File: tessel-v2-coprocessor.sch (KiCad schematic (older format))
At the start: 46 parts, among them J401 CONN_02X05, J402 USB-micro-TH, J403 MODULE_HEADER, J404 MODULE_HEADER, J405 CONN_01X01, SW401 SW_PUSH, U401 SAMD21G14A-MU, X401 FC-135

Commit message: annotated
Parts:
- gave numbers to parts that had none: 4
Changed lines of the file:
@@
 $EndComp
 $Comp
-L GND #PWR0110
+L GND #PWR408
 U 1 1 548F9730
 P 4800 8050
-F 0 "#PWR0110" H 4800 8050 30  0001 C CNN
+F 0 "#PWR408" H 4800 8050 30  0001 C CNN
 F 1 "GND" H 4800 7980 30  0001 C CNN
 F 2 "" H 4800 8050 60  0000 C CNN
@@
 $EndComp
 $Comp
-L GND #PWR0111
+L GND #PWR410
 U 1 1 548F973F
 P 6000 8100
-F 0 "#PWR0111" H 6000 8100 30  0001 C CNN
+F 0 "#PWR410" H 6000 8100 30  0001 C CNN
 F 1 "GND" H 6000 8030 30  0001 C CNN
 F 2 "" H 6000 8100 60  0000 C CNN
@@
 VDDCORE
 $Comp
-L GND #PWR0112
+L GND #PWR417
 U 1 1 548FA205
 P 9400 3700
-F 0 "#PWR0112" H 9400 3700 30  0001 C CNN
+F 0 "#PWR417" H 9400 3700 30  0001 C CNN
 F 1 "GND" H 9400 3630 30  0001 C CNN
 F 2 "" H 9400 3700 60  0000 C CNN
@@
 $EndComp
 $Comp
-L GND #PWR0113
+L GND #PWR416
 U 1 1 548FBD70
 P 9000 3700
-F 0 "#PWR0113" H 9000 3700 30  0001 C CNN
+F 0 "#PWR416" H 9000 3700 30  0001 C CNN
 F 1 "GND" H 9000 3630 30  0001 C CNN
 F 2 "" H 9000 3700 60  0000 C CNN
@@
 $EndComp
 $Comp
-L GND #PWR0114
+L GND #PWR414
 U 1 1 548FBD83
 P 7500 3700
-F 0 "#PWR0114" H 7500 3700 30  0001 C CNN
+F 0 "#PWR414" H 7500 3700 30  0001 C CNN
 F 1 "GND" H 7500 3630 30  0001 C CNN
 F 2 "" H 7500 3700 60  0000 C CNN
@@
 $EndComp
 $Comp
-L GND #PWR0115
+L GND #PWR413
 U 1 1 548FBD8A
 P 7100 3700
-F 0 "#PWR0115" H 7100 3700 30  0001 C CNN
+F 0 "#PWR413" H 7100 3700 30  0001 C CNN
 F 1 "GND" H 7100 3630 30  0001 C CNN
 F 2 "" H 7100 3700 60  0000 C CNN
@@
 $EndComp
 $Comp
-L GND #PWR0116
+L GND #PWR412
 U 1 1 548FBD9D
 P 6700 3700
-F 0 "#PWR0116" H 6700 3700 30  0001 C CNN
+F 0 "#PWR412" H 6700 3700 30  0001 C CNN
 F 1 "GND" H 6700 3630 30  0001 C CNN
 F 2 "" H 6700 3700 60  0000 C CNN
@@
 $EndComp
 $Comp
-L GND #PWR0117
+L GND #PWR411
 U 1 1 548FBDA4
 P 6300 3700
-F 0 "#PWR0117" H 6300 3700 30  0001 C CNN
+F 0 "#PWR411" H 6300 3700 30  0001 C CNN
 F 1 "GND" H 6300 3630 30  0001 C CNN
 F 2 "" H 6300 3700 60  0000 C CNN
@@
 $EndComp
 $Comp
-L GND #PWR0118
+L GND #PWR409
 U 1 1 548FBDB7
 P 5900 3700
-F 0 "#PWR0118" H 5900 3700 30  0001 C CNN
+F 0 "#PWR409" H 5900 3700 30  0001 C CNN
 F 1 "GND" H 5900 3630 30  0001 C CNN
 F 2 "" H 5900 3700 60  0000 C CNN
@@
 $EndComp
 $Comp
-L GND #PWR0119
+L GND #PWR415
 U 1 1 548FD791
 P 8000 8100
-F 0 "#PWR0119" H 8000 8100 30  0001 C CNN
+F 0 "#PWR415" H 8000 8100 30  0001 C CNN
 F 1 "GND" H 8000 8030 30  0001 C CNN
 F 2 "" H 8000 8100 60  0000 C CNN
@@
 $EndComp
 $Comp
-L GND #PWR0120
+L GND #PWR422
 U 1 1 54E6B173
 P 14600 7700
-F 0 "#PWR0120" H 14600 7700 30  0001 C CNN
+F 0 "#PWR422" H 14600 7700 30  0001 C CNN
 F 1 "GND" H 14600 7630 30  0001 C CNN
 F 2 "" H 14600 7700 60  0000 C CNN
@@
 3.3V_CP
 $Comp
-L GND #PWR0121
+L GND #PWR419
 U 1 1 54E6B4A0
 P 13600 7700
-F 0 "#PWR0121" H 13600 7700 30  0001 C CNN
+F 0 "#PWR419" H 13600 7700 30  0001 C CNN
 F 1 "GND" H 13600 7630 30  0001 C CNN
 F 2 "" H 13600 7700 60  0000 C CNN
@@
 NoConn ~ 1400 6400
 $Comp
-L GND #PWR0122
+L GND #PWR403
 U 1 1 54E6D866
 P 1300 6600
-F 0 "#PWR0122" H 1300 6350 60  0001 C CNN
+F 0 "#PWR403" H 1300 6350 60  0001 C CNN
 F 1 "GND" H 1300 6450 60  0000 C CNN
 F 2 "" H 1300 6600 60  0000 C CNN
@@
 3.3V_PORTA
 $Comp
-L GND #PWR0123
+L GND #PWR420
 U 1 1 54E753B7
 P 14200 2400
-F 0 "#PWR0123" H 14200 2150 60  0001 C CNN
+F 0 "#PWR420" H 14200 2150 60  0001 C CNN
 F 1 "GND" H 14200 2250 60  0000 C CNN
 F 2 "" H 14200 2400 60  0000 C CNN
@@
 $EndComp
 $Comp
-L GND #PWR0124
+L GND #PWR421
 U 1 1 54E753CD
 P 14300 4200
-F 0 "#PWR0124" H 14300 3950 60  0001 C CNN
+F 0 "#PWR421" H 14300 3950 60  0001 C CNN
 F 1 "GND" H 14300 4050 60  0000 C CNN
 F 2 "" H 14300 4200 60  0000 C CNN
@@
 PORT_A_G3
 $Comp
-L +5V #PWR0125
+L +5V #PWR404
 U 1 1 54E79A0D
 P 2600 1400
-F 0 "#PWR0125" H 2600 1490 20  0001 C CNN
+F 0 "#PWR404" H 2600 1490 20  0001 C CNN
 F 1 "+5V" H 2600 1550 30  0000 C CNN
 F 2 "" H 2600 1400 60  0000 C CNN
@@
 $EndComp
 $Comp
-L GND #PWR0126
+L GND #PWR405
 U 1 1 54E79A13
 P 2600 2100
-F 0 "#PWR0126" H 2600 1850 60  0001 C CNN
+F 0 "#PWR405" H 2600 1850 60  0001 C CNN
 F 1 "GND" H 2600 1950 60  0000 C CNN
 F 2 "" H 2600 2100 60  0000 C CNN
@@
 $EndComp
 $Comp
-L GND #PWR0127
+L GND #PWR406
 U 1 1 54E79A19
 P 2900 2500
-F 0 "#PWR0127" H 2900 2250 60  0001 C CNN
+F 0 "#PWR406" H 2900 2250 60  0001 C CNN
 F 1 "GND" H 2900 2350 60  0000 C CNN
 F 2 "" H 2900 2500 60  0000 C CNN
@@
 $EndComp
 $Comp
-L GND #PWR0128
+L GND #PWR401
 U 1 1 54E79A1F
 P 1300 3100
-F 0 "#PWR0128" H 1300 2850 60  0001 C CNN
+F 0 "#PWR401" H 1300 2850 60  0001 C CNN
 F 1 "GND" H 1300 2950 60  0000 C CNN
 F 2 "" H 1300 3100 60  0000 C CNN
@@
 $EndComp
 $Comp
-L +5V #PWR0129
+L +5V #PWR407
 U 1 1 54E79A2D
 P 3800 2100
-F 0 "#PWR0129" H 3800 2190 20  0001 C CNN
+F 0 "#PWR407" H 3800 2190 20  0001 C CNN
 F 1 "+5V" H 3800 2250 30  0000 C CNN
 F 2 "" H 3800 2100 60  0000 C CNN
@@
 FLASH_~CS
 $Comp
-L GND #PWR0130
+L GND #PWR418
 U 1 1 54EE1D18
 P 11600 3500
-F 0 "#PWR0130" H 11600 3250 60  0001 C CNN
+F 0 "#PWR418" H 11600 3250 60  0001 C CNN
 F 1 "GND" H 11600 3350 60  0000 C CNN
 F 2 "" H 11600 3500 60  0000 C CNN
@@
 	13500 2100 13500 2200
 $Comp
-L TP TP?
+L TP TP403
 U 1 1 55076899
 P 2400 5000
-F 0 "TP?" H 2400 5050 60  0000 C CNN
+F 0 "TP403" H 2400 5050 60  0000 C CNN
 F 1 "TP" H 2400 4950 60  0001 C CNN
 F 2 "" H 2400 5000 60  0000 C CNN
@@
 $EndComp
 $Comp
-L TP TP?
+L TP TP404
 U 1 1 55076939
 P 2400 5200
-F 0 "TP?" H 2400 5250 60  0000 C CNN
+F 0 "TP404" H 2400 5250 60  0000 C CNN
 F 1 "TP" H 2400 5150 60  0001 C CNN
 F 2 "" H 2400 5200 60  0000 C CNN
@@
 3.3V_CP
 $Comp
-L TP TP?
+L TP TP402
 U 1 1 550772D3
 P 2400 4800
-F 0 "TP?" H 2400 4850 60  0000 C CNN
+F 0 "TP402" H 2400 4850 60  0000 C CNN
 F 1 "TP" H 2400 4750 60  0001 C CNN
 F 2 "" H 2400 4800 60  0000 C CNN
@@
 	2400 4800 2000 4800
 $Comp
-L GND #PWR?
+L GND #PWR402
 U 1 1 55077307
 P 1300 4700
-F 0 "#PWR?" H 1300 4450 60  0001 C CNN
+F 0 "#PWR402" H 1300 4450 60  0001 C CNN
 F 1 "GND" H 1300 4550 60  0000 C CNN
 F 2 "" H 1300 4700 60  0000 C CNN
@@
 $EndComp
 $Comp
-L TP TP?
+L TP TP401
 U 1 1 5507734C
 P 2400 4600
-F 0 "TP?" H 2400 4650 60  0000 C CNN
+F 0 "TP401" H 2400 4650 60  0000 C CNN
 F 1 "TP" H 2400 4550 60  0001 C CNN
 F 2 "" H 2400 4600 60  0000 C CNN

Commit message: netlist, etc.
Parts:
- TP401, TP402, TP403, TP404: footprint (none) -> tm-kicad-lib:Testpoint
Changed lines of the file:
@@
 $EndComp
 $Comp
-L GND #PWR408
+L GND #PWR0113
 U 1 1 548F9730
 P 4800 8050
-F 0 "#PWR408" H 4800 8050 30  0001 C CNN
+F 0 "#PWR0113" H 4800 8050 30  0001 C CNN
 F 1 "GND" H 4800 7980 30  0001 C CNN
 F 2 "" H 4800 8050 60  0000 C CNN
@@
 $EndComp
 $Comp
-L GND #PWR410
+L GND #PWR0114
 U 1 1 548F973F
 P 6000 8100
-F 0 "#PWR410" H 6000 8100 30  0001 C CNN
+F 0 "#PWR0114" H 6000 8100 30  0001 C CNN
 F 1 "GND" H 6000 8030 30  0001 C CNN
 F 2 "" H 6000 8100 60  0000 C CNN
@@
 VDDCORE
 $Comp
-L GND #PWR417
+L GND #PWR0115
 U 1 1 548FA205
 P 9400 3700
-F 0 "#PWR417" H 9400 3700 30  0001 C CNN
+F 0 "#PWR0115" H 9400 3700 30  0001 C CNN
 F 1 "GND" H 9400 3630 30  0001 C CNN
 F 2 "" H 9400 3700 60  0000 C CNN
@@
 $EndComp
 $Comp
-L GND #PWR416
+L GND #PWR0116
 U 1 1 548FBD70
 P 9000 3700
-F 0 "#PWR416" H 9000 3700 30  0001 C CNN
+F 0 "#PWR0116" H 9000 3700 30  0001 C CNN
 F 1 "GND" H 9000 3630 30  0001 C CNN
 F 2 "" H 9000 3700 60  0000 C CNN
@@
 $EndComp
 $Comp
-L GND #PWR414
+L GND #PWR0117
 U 1 1 548FBD83
 P 7500 3700
-F 0 "#PWR414" H 7500 3700 30  0001 C CNN
+F 0 "#PWR0117" H 7500 3700 30  0001 C CNN
 F 1 "GND" H 7500 3630 30  0001 C CNN
 F 2 "" H 7500 3700 60  0000 C CNN
@@
 $EndComp
 $Comp
-L GND #PWR413
+L GND #PWR0118
 U 1 1 548FBD8A
 P 7100 3700
-F 0 "#PWR413" H 7100 3700 30  0001 C CNN
+F 0 "#PWR0118" H 7100 3700 30  0001 C CNN
 F 1 "GND" H 7100 3630 30  0001 C CNN
 F 2 "" H 7100 3700 60  0000 C CNN
@@
 $EndComp
 $Comp
-L GND #PWR412
+L GND #PWR0119
 U 1 1 548FBD9D
 P 6700 3700
-F 0 "#PWR412" H 6700 3700 30  0001 C CNN
+F 0 "#PWR0119" H 6700 3700 30  0001 C CNN
 F 1 "GND" H 6700 3630 30  0001 C CNN
 F 2 "" H 6700 3700 60  0000 C CNN
@@
 $EndComp
 $Comp
-L GND #PWR411
+L GND #PWR0120
 U 1 1 548FBDA4
 P 6300 3700
-F 0 "#PWR411" H 6300 3700 30  0001 C CNN
+F 0 "#PWR0120" H 6300 3700 30  0001 C CNN
 F 1 "GND" H 6300 3630 30  0001 C CNN
 F 2 "" H 6300 3700 60  0000 C CNN
@@
 $EndComp
 $Comp
-L GND #PWR409
+L GND #PWR0121
 U 1 1 548FBDB7
 P 5900 3700
-F 0 "#PWR409" H 5900 3700 30  0001 C CNN
+F 0 "#PWR0121" H 5900 3700 30  0001 C CNN
 F 1 "GND" H 5900 3630 30  0001 C CNN
 F 2 "" H 5900 3700 60  0000 C CNN
@@
 $EndComp
 $Comp
-L GND #PWR415
+L GND #PWR0122
 U 1 1 548FD791
 P 8000 8100
-F 0 "#PWR415" H 8000 8100 30  0001 C CNN
+F 0 "#PWR0122" H 8000 8100 30  0001 C CNN
 F 1 "GND" H 8000 8030 30  0001 C CNN
 F 2 "" H 8000 8100 60  0000 C CNN
@@
 $EndComp
 $Comp
-L GND #PWR422
+L GND #PWR0123
 U 1 1 54E6B173
 P 14600 7700
-F 0 "#PWR422" H 14600 7700 30  0001 C CNN
+F 0 "#PWR0123" H 14600 7700 30  0001 C CNN
 F 1 "GND" H 14600 7630 30  0001 C CNN
 F 2 "" H 14600 7700 60  0000 C CNN
@@
 3.3V_CP
 $Comp
-L GND #PWR419
+L GND #PWR0124
 U 1 1 54E6B4A0
 P 13600 7700
-F 0 "#PWR419" H 13600 7700 30  0001 C CNN
+F 0 "#PWR0124" H 13600 7700 30  0001 C CNN
 F 1 "GND" H 13600 7630 30  0001 C CNN
 F 2 "" H 13600 7700 60  0000 C CNN
@@
 NoConn ~ 1400 6400
 $Comp
-L GND #PWR403
+L GND #PWR0125
 U 1 1 54E6D866
 P 1300 6600
-F 0 "#PWR403" H 1300 6350 60  0001 C CNN
+F 0 "#PWR0125" H 1300 6350 60  0001 C CNN
 F 1 "GND" H 1300 6450 60  0000 C CNN
 F 2 "" H 1300 6600 60  0000 C CNN
@@
 3.3V_PORTA
 $Comp
-L GND #PWR420
+L GND #PWR0126
 U 1 1 54E753B7
 P 14200 2400
-F 0 "#PWR420" H 14200 2150 60  0001 C CNN
+F 0 "#PWR0126" H 14200 2150 60  0001 C CNN
 F 1 "GND" H 14200 2250 60  0000 C CNN
 F 2 "" H 14200 2400 60  0000 C CNN
@@
 $EndComp
 $Comp
-L GND #PWR421
+L GND #PWR0127
 U 1 1 54E753CD
 P 14300 4200
-F 0 "#PWR421" H 14300 3950 60  0001 C CNN
+F 0 "#PWR0127" H 14300 3950 60  0001 C CNN
 F 1 "GND" H 14300 4050 60  0000 C CNN
 F 2 "" H 14300 4200 60  0000 C CNN
@@
 PORT_A_G3
 $Comp
-L +5V #PWR404
+L +5V #PWR0128
 U 1 1 54E79A0D
 P 2600 1400
-F 0 "#PWR404" H 2600 1490 20  0001 C CNN
+F 0 "#PWR0128" H 2600 1490 20  0001 C CNN
 F 1 "+5V" H 2600 1550 30  0000 C CNN
 F 2 "" H 2600 1400 60  0000 C CNN
@@
 $EndComp
 $Comp
-L GND #PWR405
+L GND #PWR0129
 U 1 1 54E79A13
 P 2600 2100
-F 0 "#PWR405" H 2600 1850 60  0001 C CNN
+F 0 "#PWR0129" H 2600 1850 60  0001 C CNN
 F 1 "GND" H 2600 1950 60  0000 C CNN
 F 2 "" H 2600 2100 60  0000 C CNN
@@
 $EndComp
 $Comp
-L GND #PWR406
+L GND #PWR0130
 U 1 1 54E79A19
 P 2900 2500
-F 0 "#PWR406" H 2900 2250 60  0001 C CNN
+F 0 "#PWR0130" H 2900 2250 60  0001 C CNN
 F 1 "GND" H 2900 2350 60  0000 C CNN
 F 2 "" H 2900 2500 60  0000 C CNN
@@
 $EndComp
 $Comp
-L GND #PWR401
+L GND #PWR0131
 U 1 1 54E79A1F
 P 1300 3100
-F 0 "#PWR401" H 1300 2850 60  0001 C CNN
+F 0 "#PWR0131" H 1300 2850 60  0001 C CNN
 F 1 "GND" H 1300 2950 60  0000 C CNN
 F 2 "" H 1300 3100 60  0000 C CNN
@@
 $EndComp
 $Comp
-L +5V #PWR407
+L +5V #PWR0132
 U 1 1 54E79A2D
 P 3800 2100
-F 0 "#PWR407" H 3800 2190 20  0001 C CNN
+F 0 "#PWR0132" H 3800 2190 20  0001 C CNN
 F 1 "+5V" H 3800 2250 30  0000 C CNN
 F 2 "" H 3800 2100 60  0000 C CNN
@@
 FLASH_~CS
 $Comp
-L GND #PWR418
+L GND #PWR0133
 U 1 1 54EE1D18
 P 11600 3500
-F 0 "#PWR418" H 11600 3250 60  0001 C CNN
+F 0 "#PWR0133" H 11600 3250 60  0001 C CNN
 F 1 "GND" H 11600 3350 60  0000 C CNN
 F 2 "" H 11600 3500 60  0000 C CNN
@@
 F 0 "TP403" H 2400 5050 60  0000 C CNN
 F 1 "TP" H 2400 4950 60  0001 C CNN
-F 2 "" H 2400 5000 60  0000 C CNN
+F 2 "tm-kicad-lib:Testpoint" H 2400 5000 60  0001 C CNN
 F 3 "" H 2400 5000 60  0000 C CNN
 	1    2400 5000
@@
 F 0 "TP404" H 2400 5250 60  0000 C CNN
 F 1 "TP" H 2400 5150 60  0001 C CNN
-F 2 "" H 2400 5200 60  0000 C CNN
+F 2 "tm-kicad-lib:Testpoint" H 2400 5200 60  0001 C CNN
 F 3 "" H 2400 5200 60  0000 C CNN
 	1    2400 5200
@@
 F 0 "TP402" H 2400 4850 60  0000 C CNN
 F 1 "TP" H 2400 4750 60  0001 C CNN
-F 2 "" H 2400 4800 60  0000 C CNN
+F 2 "tm-kicad-lib:Testpoint" H 2400 4800 60  0001 C CNN
 F 3 "" H 2400 4800 60  0000 C CNN
 	1    2400 4800
@@
 	2400 4800 2000 4800
 $Comp
-L GND #PWR402
+L GND #PWR0134
 U 1 1 55077307
 P 1300 4700
-F 0 "#PWR402" H 1300 4450 60  0001 C CNN
+F 0 "#PWR0134" H 1300 4450 60  0001 C CNN
 F 1 "GND" H 1300 4550 60  0000 C CNN
 F 2 "" H 1300 4700 60  0000 C CNN
@@
 F 0 "TP401" H 2400 4650 60  0000 C CNN
 F 1 "TP" H 2400 4550 60  0001 C CNN
-F 2 "" H 2400 4600 60  0000 C CNN
+F 2 "tm-kicad-lib:Testpoint" H 2400 4600 60  0001 C CNN
 F 3 "" H 2400 4600 60  0000 C CNN
 	1    2400 4600

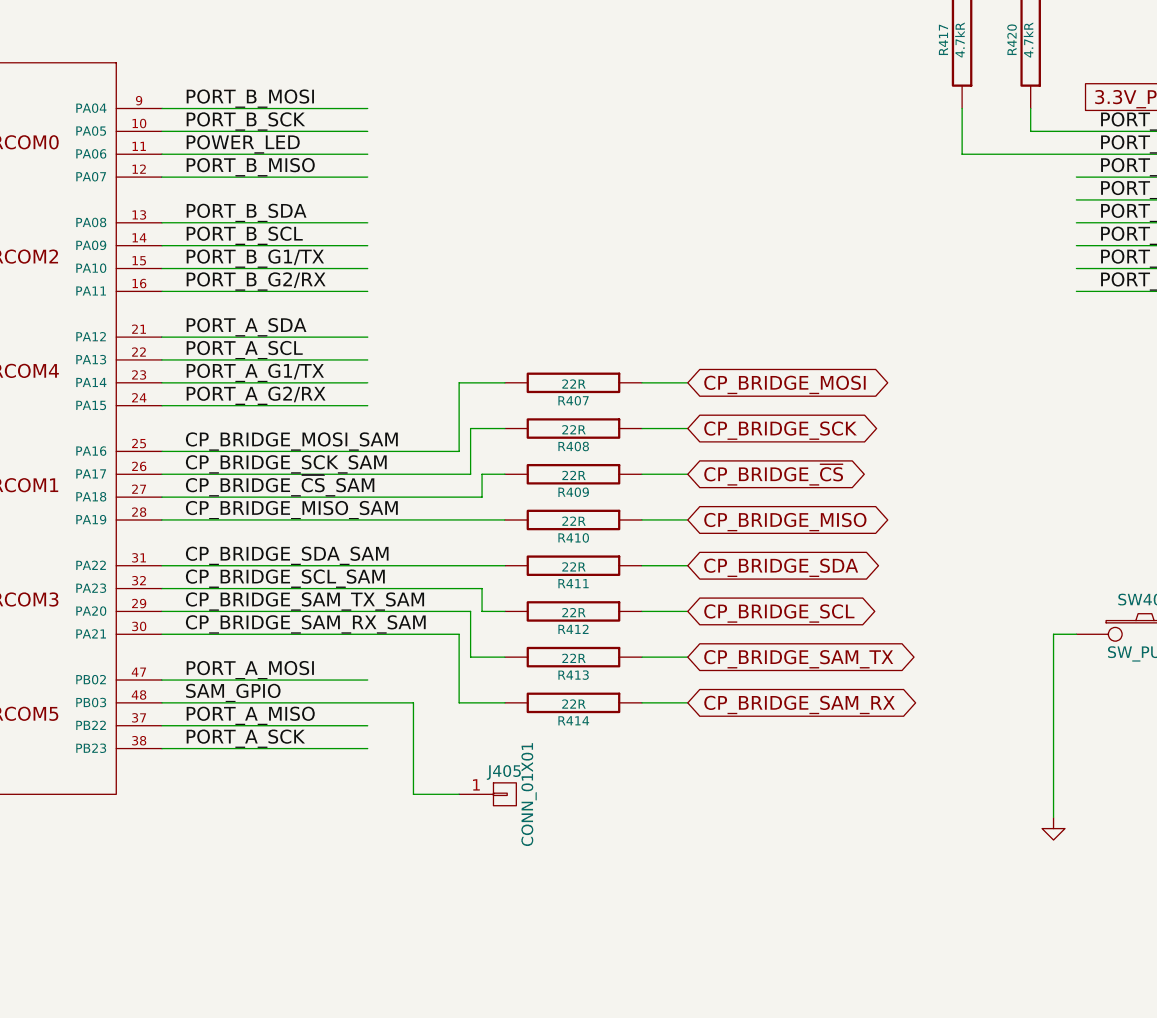
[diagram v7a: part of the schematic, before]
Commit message: added 10k pu to sam !cs
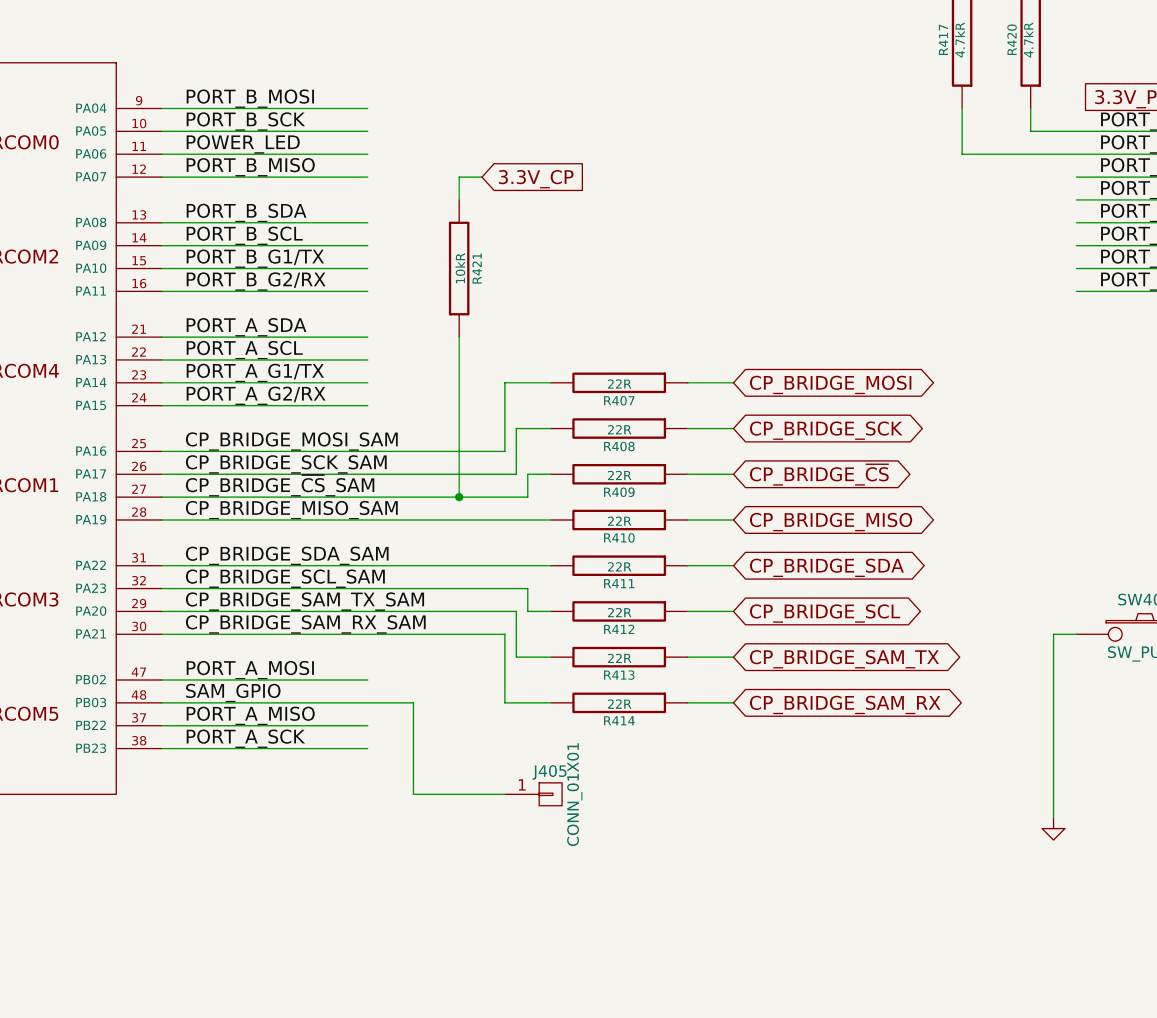
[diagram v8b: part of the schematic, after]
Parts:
- added R421: 10kR, tm-kicad-lib:SMD-0402-R, symbol TM_R
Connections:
- wire segments 209 -> 212
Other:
- moved on the sheet: J405, R407, R408, R409, R410, R411, R412, R413, R414
